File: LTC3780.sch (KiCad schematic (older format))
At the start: 54 parts, among them Q2 BSC340N08NS3G, Q3 BSC340N08NS3G, Q4 BSC340N08NS3G, Q5 BSC340N08NS3G, U1 LTC3780EGPBF

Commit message: Footprints added
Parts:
- C1, C10, C11, C12, C13, C14, C15, C16, C17, C18, C19, C2, C20, C21, C22, C23, C3, C4, C5, C6, C9: footprint (none) -> Capacitors_SMD:C_0603_HandSoldering
- CIN1: footprint (none) -> Capacitors_SMD:CP_Elec_8x6.7
- COUT1: footprint (none) -> Capacitors_SMD:CP_Elec_8x10.5
- R1, R10, R11, R12, R13, R14, R15, R16, R17, R2, R20, R21, R4, R5, R8, R9: footprint (none) -> Resistors_SMD:R_0603_HandSoldering
- R18, R19: footprint (none) -> Resistors_SMD:R_2512_HandSoldering
- U1: footprint SOP65P780X200-24N -> LTC3780EGPBF:SOP65P780X200-24N

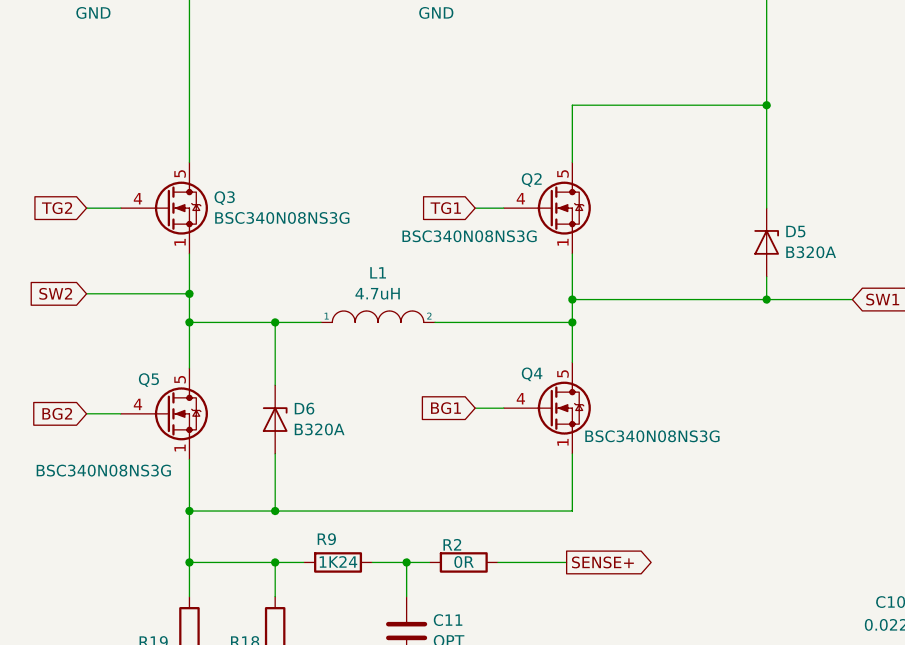
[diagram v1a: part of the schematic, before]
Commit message: Added Different Switching MOSFET
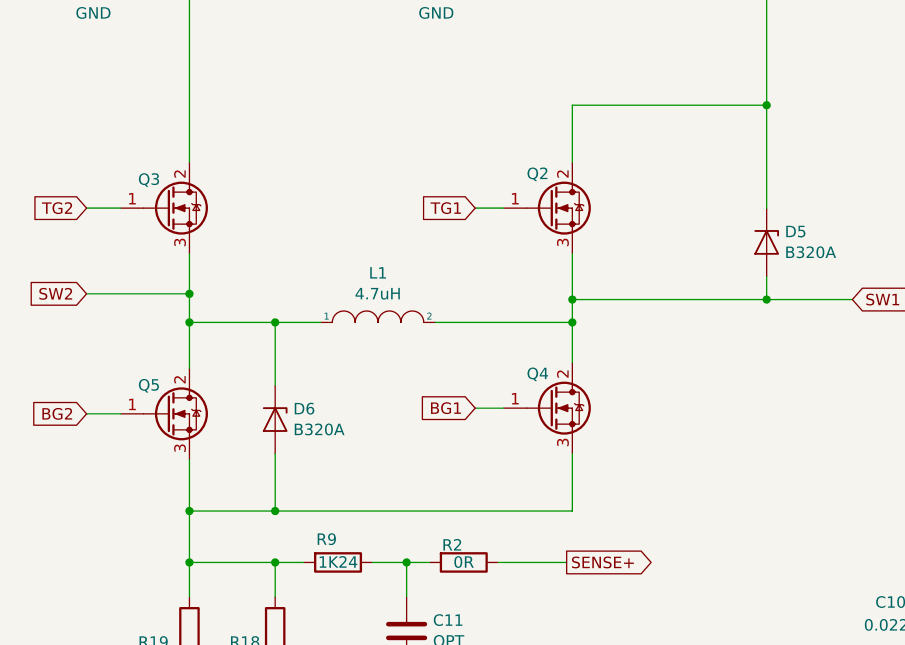
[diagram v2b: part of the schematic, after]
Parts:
- removed Q2, Q3, Q4, Q5: BSC340N08NS3G, TO_SOT_Packages_SMD:TO-252-2, symbol Transistor_FET:BSC340N08NS3G
- added Q2, Q3, Q4, Q5: IPD100N04S402ATMA1, TO_SOT_Packages_SMD:TO-252-2, symbol Transistor_FET:IPD100N04S402ATMA1
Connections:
- net +VSW: now also Q3.2
- net BG1: now also Q4.1
- net BG2: now also Q5.1
- net SW1: now also Q2.3, Q4.2
- net SW2: now also Q3.3, Q5.2
- net TG1: now also Q2.1
- net TG2: now also Q3.1
- net VCC: now also Q2.2
- net at D6.2 (A), R18.1, R19.1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: now also Q4.3, Q5.3
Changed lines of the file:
@@
 Wire Wire Line
 	1275 5075 1650 5075
-$Comp
-L Transistor_FET:BSC340N08NS3G Q5
-U 1 1 5CB21D35
-P 1175 3775
-F 0 "Q5" H 1050 3925 50  0000 L CNN
-F 1 "BSC340N08NS3G" H 600 3525 50  0000 L CNN
-F 2 "TO_SOT_Packages_SMD:TO-252-2" H 1375 3700 50  0001 L CIN
-F 3 "http://www.infineon.com/dgdl/Infineon-BSC340N08NS3G-DS-v02_06-en.pdf?fileId=db3a30431add1d95011ae81c21f2563a" V 1175 3775 50  0001 L CNN
-	1    1175 3775
-	1    0    0    -1
-$EndComp
-$Comp
-L Transistor_FET:BSC340N08NS3G Q3
-U 1 1 5CB28B91
-P 1175 2875
-F 0 "Q3" H 1381 2921 50  0000 L CNN
-F 1 "BSC340N08NS3G" H 1381 2830 50  0000 L CNN
-F 2 "TO_SOT_Packages_SMD:TO-252-2" H 1375 2800 50  0001 L CIN
-F 3 "http://www.infineon.com/dgdl/Infineon-BSC340N08NS3G-DS-v02_06-en.pdf?fileId=db3a30431add1d95011ae81c21f2563a" V 1175 2875 50  0001 L CNN
-	1    1175 2875
-	1    0    0    -1
-$EndComp
-$Comp
-L Transistor_FET:BSC340N08NS3G Q4
-U 1 1 5CB2DC26
-P 2850 3750
-F 0 "Q4" H 2725 3900 50  0000 L CNN
-F 1 "BSC340N08NS3G" H 3000 3625 50  0000 L CNN
-F 2 "TO_SOT_Packages_SMD:TO-252-2" H 3050 3675 50  0001 L CIN
-F 3 "http://www.infineon.com/dgdl/Infineon-BSC340N08NS3G-DS-v02_06-en.pdf?fileId=db3a30431add1d95011ae81c21f2563a" V 2850 3750 50  0001 L CNN
-	1    2850 3750
-	1    0    0    -1
-$EndComp
-$Comp
-L Transistor_FET:BSC340N08NS3G Q2
-U 1 1 5CB36037
-P 2850 2875
-F 0 "Q2" H 2725 3000 50  0000 L CNN
-F 1 "BSC340N08NS3G" H 2200 2750 50  0000 L CNN
-F 2 "TO_SOT_Packages_SMD:TO-252-2" H 3050 2800 50  0001 L CIN
-F 3 "http://www.infineon.com/dgdl/Infineon-BSC340N08NS3G-DS-v02_06-en.pdf?fileId=db3a30431add1d95011ae81c21f2563a" V 2850 2875 50  0001 L CNN
-	1    2850 2875
-	1    0    0    -1
-$EndComp
 Text GLabel 825  3775 0    50   Input ~ 0
 BG2
@@
 Wire Wire Line
 	8050 4775 8350 4775
+$Comp
+L Transistor_FET:IPD100N04S402ATMA1 Q5
+U 1 1 5CB2C8BA
+P 1275 3775
+F 0 "Q5" H 1050 3900 50  0000 L CNN
+F 1 "IPD100N04S402ATMA1" H 525 3550 50  0001 L CNN
+F 2 "TO_SOT_Packages_SMD:TO-252-2" H 1275 3775 50  0001 C CNN
+F 3 "https://www.infineon.com/dgdl/Infineon-IPD100N04S4_02-DS-v01_00-en.pdf?fileId=db3a304328c6bd5c01291c8301be5e3f" H 1275 3775 50  0001 C CNN
+	1    1275 3775
+	1    0    0    -1
+$EndComp
+$Comp
+L Transistor_FET:IPD100N04S402ATMA1 Q3
+U 1 1 5CB2E058
+P 1275 2875
+F 0 "Q3" H 1050 3000 50  0000 L CNN
+F 1 "IPD100N04S402ATMA1" H 575 2650 50  0001 L CNN
+F 2 "TO_SOT_Packages_SMD:TO-252-2" H 1275 2875 50  0001 C CNN
+F 3 "https://www.infineon.com/dgdl/Infineon-IPD100N04S4_02-DS-v01_00-en.pdf?fileId=db3a304328c6bd5c01291c8301be5e3f" H 1275 2875 50  0001 C CNN
+	1    1275 2875
+	1    0    0    -1
+$EndComp
+$Comp
+L Transistor_FET:IPD100N04S402ATMA1 Q2
+U 1 1 5CB2E693
+P 2950 2875
+F 0 "Q2" H 2750 3025 50  0000 L CNN
+F 1 "IPD100N04S402ATMA1" H 3056 2830 50  0001 L CNN
+F 2 "TO_SOT_Packages_SMD:TO-252-2" H 2950 2875 50  0001 C CNN
+F 3 "https://www.infineon.com/dgdl/Infineon-IPD100N04S4_02-DS-v01_00-en.pdf?fileId=db3a304328c6bd5c01291c8301be5e3f" H 2950 2875 50  0001 C CNN
+	1    2950 2875
+	1    0    0    -1
+$EndComp
+$Comp
+L Transistor_FET:IPD100N04S402ATMA1 Q4
+U 1 1 5CB2ED02
+P 2950 3750
+F 0 "Q4" H 2750 3900 50  0000 L CNN
+F 1 "IPD100N04S402ATMA1" H 3056 3705 50  0001 L CNN
+F 2 "TO_SOT_Packages_SMD:TO-252-2" H 2950 3750 50  0001 C CNN
+F 3 "https://www.infineon.com/dgdl/Infineon-IPD100N04S4_02-DS-v01_00-en.pdf?fileId=db3a304328c6bd5c01291c8301be5e3f" H 2950 3750 50  0001 C CNN
+	1    2950 3750
+	1    0    0    -1
+$EndComp
 $EndSCHEMATC

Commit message: Updated to include connector
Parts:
- added J1, J2: Screw_Terminal_01x02, Connectors_JST:JST_VH_B2P-VH_2x3.96mm_Vertical, symbol Connector:Screw_Terminal_01x02
- D1: footprint (none) -> Diodes_SMD:D_SOD-323_HandSoldering
- D3: footprint (none) -> Diodes_SMD:D_SOT-23_ANK
- D4, D7: footprint (none) -> Diodes_SMD:D_SOD-123
- D5, D6: footprint (none) -> Diodes_SMD:D_SMA_Handsoldering
- L1: footprint (none) -> Inductors:Inductor_Wurth_MAPI-4020
- PLL_IN1: footprint (none) -> Measurement_Points:Test_Point
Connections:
- net +VSW: now also J1.2 (Pin_2)
- net GND: now also J1.1 (Pin_1), J2.1 (Pin_1)
- net VCC: now also J2.2 (Pin_2)
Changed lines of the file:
@@
 encoding utf-8
 Sheet 1 1
-Title ""
-Date ""
-Rev ""
-Comp ""
+Title "LT3780 BuckBoost Circuit"
+Date "2019-04-27"
+Rev "1.0"
+Comp "tinoest"
 Comment1 ""
 Comment2 ""
@@
 F 0 "PLL_IN1" V 8200 4925 50  0000 C CNN
 F 1 "TestPoint" V 8175 5325 50  0000 C CNN
-F 2 "" H 8375 4975 50  0001 C CNN
+F 2 "Measurement_Points:Test_Point" H 8375 4975 50  0001 C CNN
 F 3 "~" H 8375 4975 50  0001 C CNN
 	1    8175 4975
@@
 F 0 "D1" V 6504 5554 50  0000 L CNN
 F 1 "4.7V" V 6595 5554 50  0000 L CNN
-F 2 "" H 6550 5475 50  0001 C CNN
+F 2 "Diodes_SMD:D_SOD-323_HandSoldering" H 6550 5475 50  0001 C CNN
 F 3 "~" H 6550 5475 50  0001 C CNN
 	1    6550 5475
@@
 F 0 "D4" V 6996 2346 50  0000 R CNN
 F 1 "1N819HW" V 6905 2346 50  0000 R CNN
-F 2 "" H 6950 2425 50  0001 C CNN
+F 2 "Diodes_SMD:D_SOD-123" H 6950 2425 50  0001 C CNN
 F 3 "~" H 6950 2425 50  0001 C CNN
 	1    6950 2425
@@
 F 0 "D7" V 6446 2346 50  0000 R CNN
 F 1 "1N819HW" V 6355 2346 50  0000 R CNN
-F 2 "" H 6400 2425 50  0001 C CNN
+F 2 "Diodes_SMD:D_SOD-123" H 6400 2425 50  0001 C CNN
 F 3 "~" H 6400 2425 50  0001 C CNN
 	1    6400 2425
@@
 F 0 "L1" H 2100 3590 50  0000 C CNN
 F 1 "4.7uH" H 2100 3499 50  0000 C CNN
-F 2 "" H 2100 3375 50  0001 C CNN
+F 2 "Inductors:Inductor_Wurth_MAPI-4020" H 2100 3375 50  0001 C CNN
 F 3 "~" H 2100 3375 50  0001 C CNN
 	1    2100 3375
@@
 F 0 "D6" V 1604 3879 50  0000 L CNN
 F 1 "B320A" V 1695 3879 50  0000 L CNN
-F 2 "" H 1650 3800 50  0001 C CNN
+F 2 "Diodes_SMD:D_SMA_Handsoldering" H 1650 3800 50  0001 C CNN
 F 3 "~" H 1650 3800 50  0001 C CNN
 	1    1650 3800
@@
 F 0 "D5" V 3754 3104 50  0000 L CNN
 F 1 "B320A" V 3845 3104 50  0000 L CNN
-F 2 "" H 3800 3025 50  0001 C CNN
+F 2 "Diodes_SMD:D_SMA_Handsoldering" H 3800 3025 50  0001 C CNN
 F 3 "~" H 3800 3025 50  0001 C CNN
 	1    3800 3025
@@
 F 0 "D3" V 804 1304 50  0000 L CNN
 F 1 "36V" V 895 1304 50  0000 L CNN
-F 2 "" H 850 1225 50  0001 C CNN
+F 2 "Diodes_SMD:D_SOT-23_ANK" H 850 1225 50  0001 C CNN
 F 3 "~" H 850 1225 50  0001 C CNN
 	1    850  1225
@@
 	1    0    0    -1
 $EndComp
+$Comp
+L Connector:Screw_Terminal_01x02 J1
+U 1 1 5CC87663
+P 800 6150
+F 0 "J1" H 718 5825 50  0000 C CNN
+F 1 "Screw_Terminal_01x02" H 718 5916 50  0000 C CNN
+F 2 "Connectors_JST:JST_VH_B2P-VH_2x3.96mm_Vertical" H 800 6150 50  0001 C CNN
+F 3 "~" H 800 6150 50  0001 C CNN
+	1    800  6150
+	-1   0    0    1
+$EndComp
+$Comp
+L Connector:Screw_Terminal_01x02 J2
+U 1 1 5CC8959A
+P 950 7200
+F 0 "J2" H 868 6875 50  0000 C CNN
+F 1 "Screw_Terminal_01x02" H 868 6966 50  0000 C CNN
+F 2 "Connectors_JST:JST_VH_B2P-VH_2x3.96mm_Vertical" H 950 7200 50  0001 C CNN
+F 3 "~" H 950 7200 50  0001 C CNN
+	1    950  7200
+	-1   0    0    1
+$EndComp
+$Comp
+L power:GND #PWR0120
+U 1 1 5CC8ABEB
+P 1650 7350
+F 0 "#PWR0120" H 1650 7100 50  0001 C CNN
+F 1 "GND" H 1655 7177 50  0000 C CNN
+F 2 "" H 1650 7350 50  0001 C CNN
+F 3 "" H 1650 7350 50  0001 C CNN
+	1    1650 7350
+	1    0    0    -1
+$EndComp
+$Comp
+L power:GND #PWR0121
+U 1 1 5CC8B727
+P 1500 6325
+F 0 "#PWR0121" H 1500 6075 50  0001 C CNN
+F 1 "GND" H 1505 6152 50  0000 C CNN
+F 2 "" H 1500 6325 50  0001 C CNN
+F 3 "" H 1500 6325 50  0001 C CNN
+	1    1500 6325
+	1    0    0    -1
+$EndComp
+$Comp
+L power:VCC #PWR0122
+U 1 1 5CC8D15D
+P 1650 6925
+F 0 "#PWR0122" H 1650 6775 50  0001 C CNN
+F 1 "VCC" H 1667 7098 50  0000 C CNN
+F 2 "" H 1650 6925 50  0001 C CNN
+F 3 "" H 1650 6925 50  0001 C CNN
+	1    1650 6925
+	1    0    0    -1
+$EndComp
+Wire Wire Line
+	1150 7200 1650 7200
+Wire Wire Line
+	1650 7200 1650 7350
+Wire Wire Line
+	1150 7100 1650 7100
+Wire Wire Line
+	1650 6925 1650 7100
+$Comp
+L power:+VSW #PWR0123
+U 1 1 5CCC4837
+P 1500 5850
+F 0 "#PWR0123" H 1500 5700 50  0001 C CNN
+F 1 "+VSW" H 1515 6023 50  0000 C CNN
+F 2 "" H 1500 5850 50  0001 C CNN
+F 3 "" H 1500 5850 50  0001 C CNN
+	1    1500 5850
+	1    0    0    -1
+$EndComp
+Wire Wire Line
+	1500 6150 1500 6325
+Wire Wire Line
+	1000 6150 1500 6150
+Wire Wire Line
+	1000 6050 1500 6050
+Wire Wire Line
+	1500 6050 1500 5850
 $EndSCHEMATC

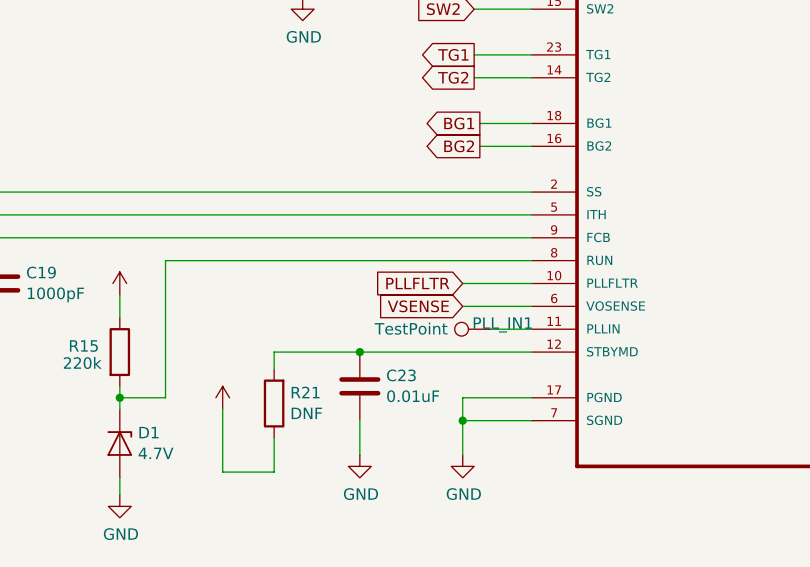
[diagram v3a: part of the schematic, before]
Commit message: Finished PCB first layout and routing, generated gerber files
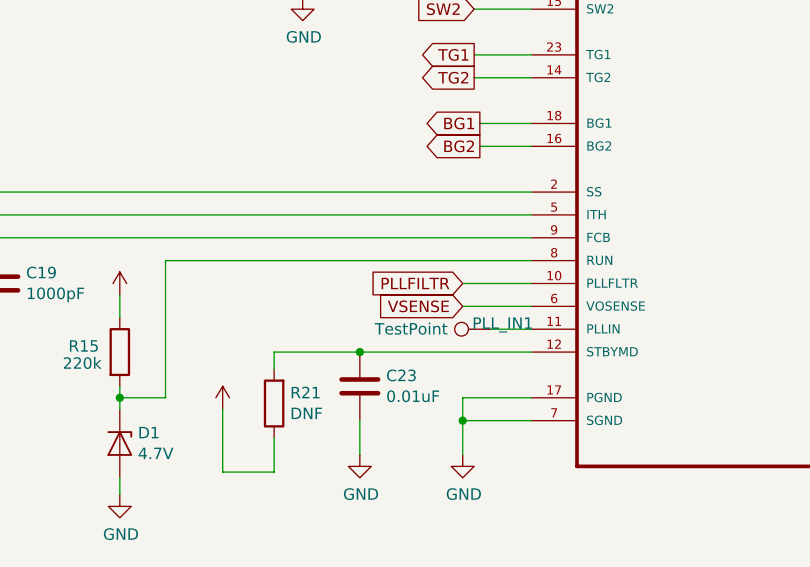
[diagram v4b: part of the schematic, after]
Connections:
- net PLLFLTR is gone; now on net PLLFILTR: U1.10 (PLLFLTR)
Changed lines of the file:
@@
 	6550 5625 6550 5700
 Text GLabel 8050 4775 0    50   Input ~ 0
-PLLFLTR
+PLLFILTR
 Text GLabel 5075 6475 0    50   Output ~ 0
 PLLFILTR

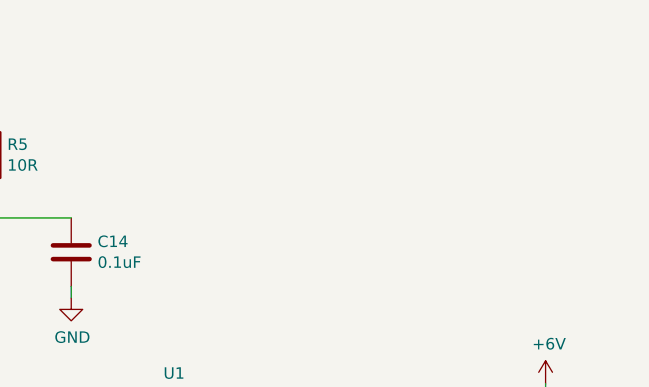
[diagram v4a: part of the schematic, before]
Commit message: Updated PCB, added routing holes and reordered some components.
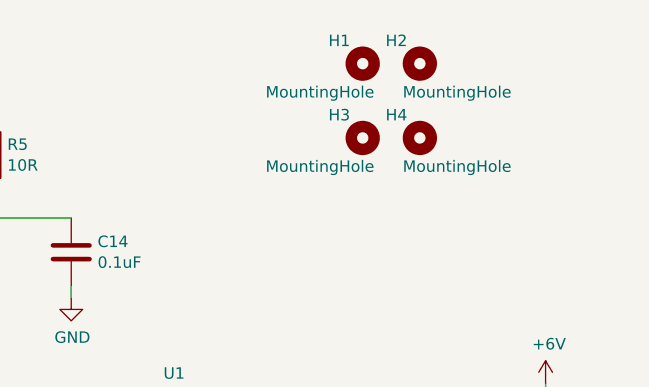
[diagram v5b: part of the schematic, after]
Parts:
- added H1, H2, H3, H4: MountingHole, Mounting_Holes:MountingHole_4mm, symbol Mechanical:MountingHole
- PLL_IN1: footprint Measurement_Points:Test_Point -> Measurement_Points:Measurement_Point_Square-SMD-Pad_Small
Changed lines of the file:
@@
 F 0 "PLL_IN1" V 8200 4925 50  0000 C CNN
 F 1 "TestPoint" V 8175 5325 50  0000 C CNN
-F 2 "Measurement_Points:Test_Point" H 8375 4975 50  0001 C CNN
+F 2 "Measurement_Points:Measurement_Point_Square-SMD-Pad_Small" H 8375 4975 50  0001 C CNN
 F 3 "~" H 8375 4975 50  0001 C CNN
 	1    8175 4975
@@
 Wire Wire Line
 	1500 6050 1500 5850
+$Comp
+L Mechanical:MountingHole H1
+U 1 1 5CDC3A6E
+P 9975 750
+F 0 "H1" H 9825 850 50  0000 L CNN
+F 1 "MountingHole" H 9550 625 50  0000 L CNN
+F 2 "Mounting_Holes:MountingHole_4mm" H 9975 750 50  0001 C CNN
+F 3 "~" H 9975 750 50  0001 C CNN
+	1    9975 750
+	1    0    0    -1
+$EndComp
+$Comp
+L Mechanical:MountingHole H2
+U 1 1 5CDC502A
+P 10225 750
+F 0 "H2" H 10075 850 50  0000 L CNN
+F 1 "MountingHole" H 10150 625 50  0000 L CNN
+F 2 "Mounting_Holes:MountingHole_4mm" H 10225 750 50  0001 C CNN
+F 3 "~" H 10225 750 50  0001 C CNN
+	1    10225 750
+	1    0    0    -1
+$EndComp
+$Comp
+L Mechanical:MountingHole H3
+U 1 1 5CDC5763
+P 9975 1075
+F 0 "H3" H 9825 1175 50  0000 L CNN
+F 1 "MountingHole" H 9550 950 50  0000 L CNN
+F 2 "Mounting_Holes:MountingHole_4mm" H 9975 1075 50  0001 C CNN
+F 3 "~" H 9975 1075 50  0001 C CNN
+	1    9975 1075
+	1    0    0    -1
+$EndComp
+$Comp
+L Mechanical:MountingHole H4
+U 1 1 5CDC622D
+P 10225 1075
+F 0 "H4" H 10075 1175 50  0000 L CNN
+F 1 "MountingHole" H 10150 950 50  0000 L CNN
+F 2 "Mounting_Holes:MountingHole_4mm" H 10225 1075 50  0001 C CNN
+F 3 "~" H 10225 1075 50  0001 C CNN
+	1    10225 1075
+	1    0    0    -1
+$EndComp
 $EndSCHEMATC

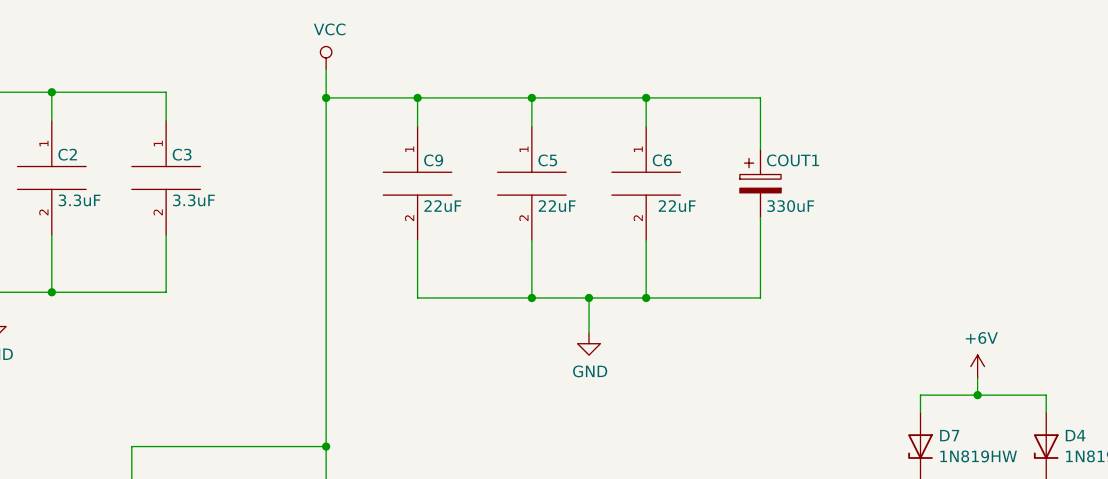
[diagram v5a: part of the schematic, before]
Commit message: Added additional Capacitor, corrected drill sizes
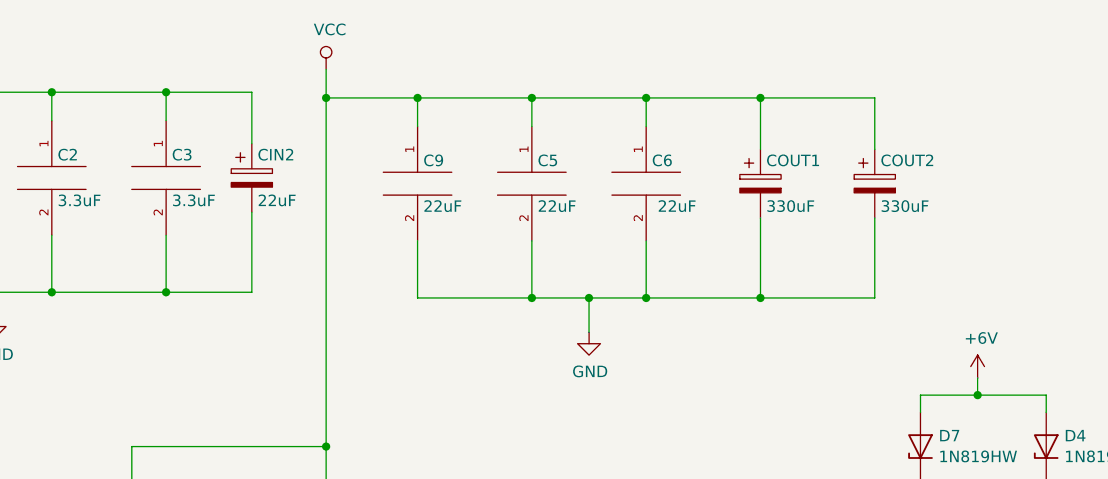
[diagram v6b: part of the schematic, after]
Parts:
- added CIN2: 22uF, Capacitors_SMD:CP_Elec_8x6.7, symbol Device:CP
- added COUT2: 330uF, Capacitors_SMD:CP_Elec_8x10.5, symbol Device:CP
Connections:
- net +VSW: now also CIN2.1
- net GND: now also CIN2.2, COUT2.2
- net VCC: now also COUT2.1
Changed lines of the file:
@@
 	1    0    0    -1
 $EndComp
+$Comp
+L Device:CP COUT2
+U 1 1 5CDD6C5E
+P 6200 1275
+F 0 "COUT2" H 6225 1375 50  0000 L CNN
+F 1 "330uF" H 6225 1175 50  0000 L CNN
+F 2 "Capacitors_SMD:CP_Elec_8x10.5" H 6238 1125 50  0001 C CNN
+F 3 "~" H 6200 1275 50  0001 C CNN
+	1    6200 1275
+	1    0    0    -1
+$EndComp
+$Comp
+L Device:CP CIN2
+U 1 1 5CDD8390
+P 3475 1250
+F 0 "CIN2" H 3500 1350 50  0000 L CNN
+F 1 "22uF" H 3500 1150 50  0000 L CNN
+F 2 "Capacitors_SMD:CP_Elec_8x6.7" H 3513 1100 50  0001 C CNN
+F 3 "~" H 3475 1250 50  0001 C CNN
+	1    3475 1250
+	1    0    0    -1
+$EndComp
+Wire Wire Line
+	3475 1100 3475 875
+Wire Wire Line
+	3475 875  3100 875
+Connection ~ 3100 875
+Wire Wire Line
+	3475 1400 3475 1750
+Wire Wire Line
+	3475 1750 3100 1750
+Connection ~ 3100 1750
+Wire Wire Line
+	6200 1125 6200 900
+Wire Wire Line
+	6200 900  5700 900
+Connection ~ 5700 900
+Wire Wire Line
+	6200 1425 6200 1775
+Wire Wire Line
+	6200 1775 5700 1775
+Connection ~ 5700 1775
 $EndSCHEMATC
